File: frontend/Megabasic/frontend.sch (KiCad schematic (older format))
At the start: 26 parts, among them CN1 EDGE, J1 CONN_02X01, J2 CONN_02X01, P1 CONN_01X02, P2 CONN_01X02, P3 CONN_01X12, P4 Control for Megaband, Q1 FDV301, T1 4:1, T2 8:1, U1 4050, U2 74LS145

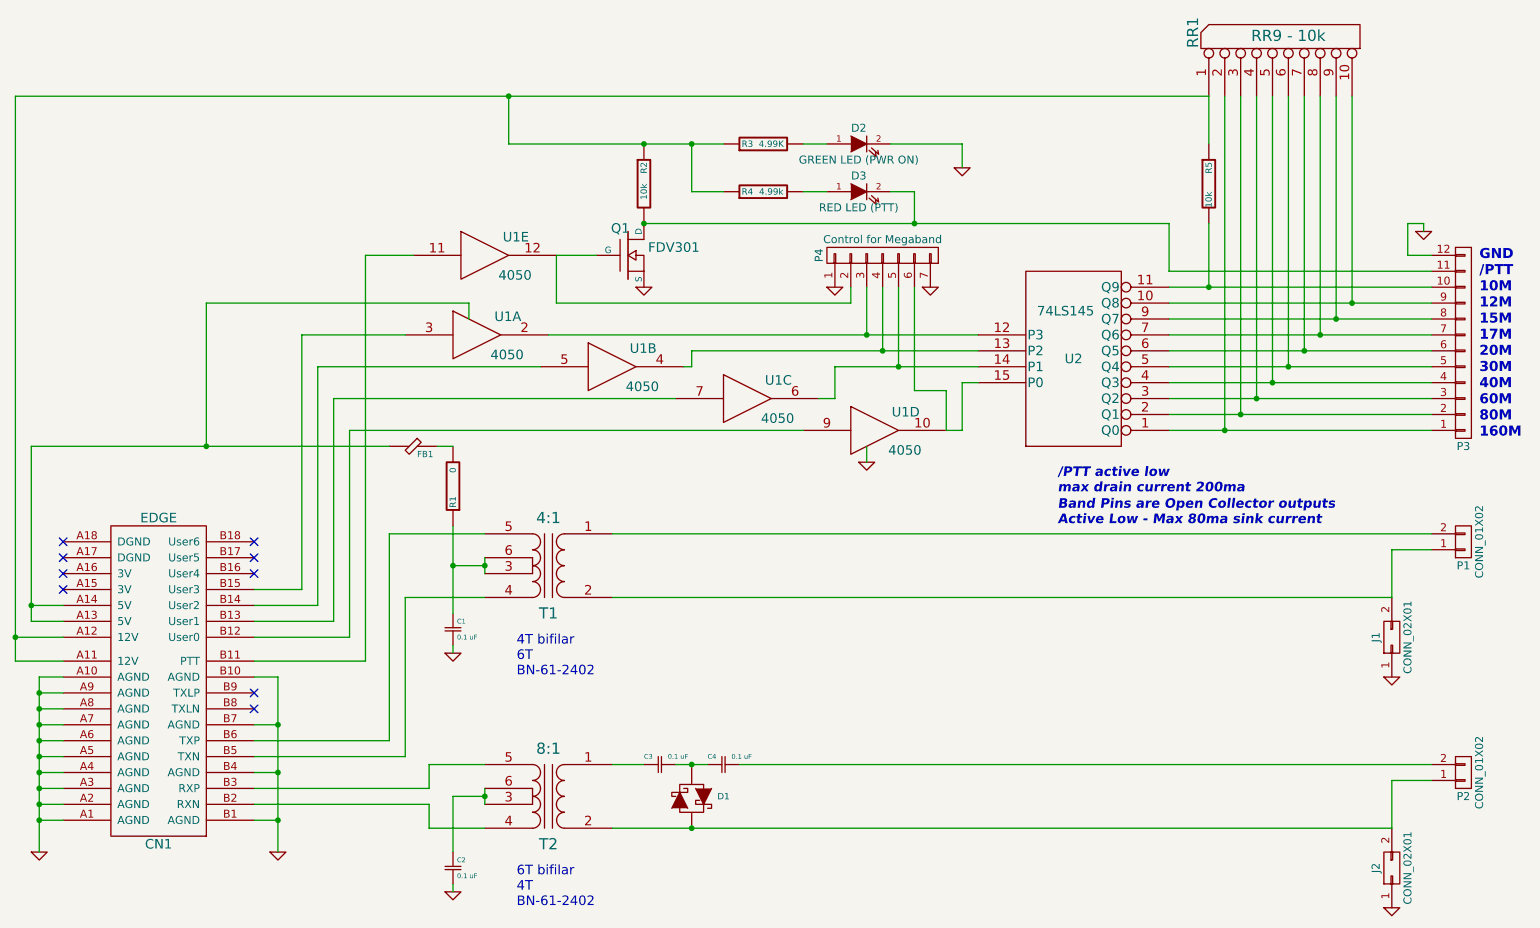
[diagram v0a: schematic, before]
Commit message: Further updates to the pre-V2 amp
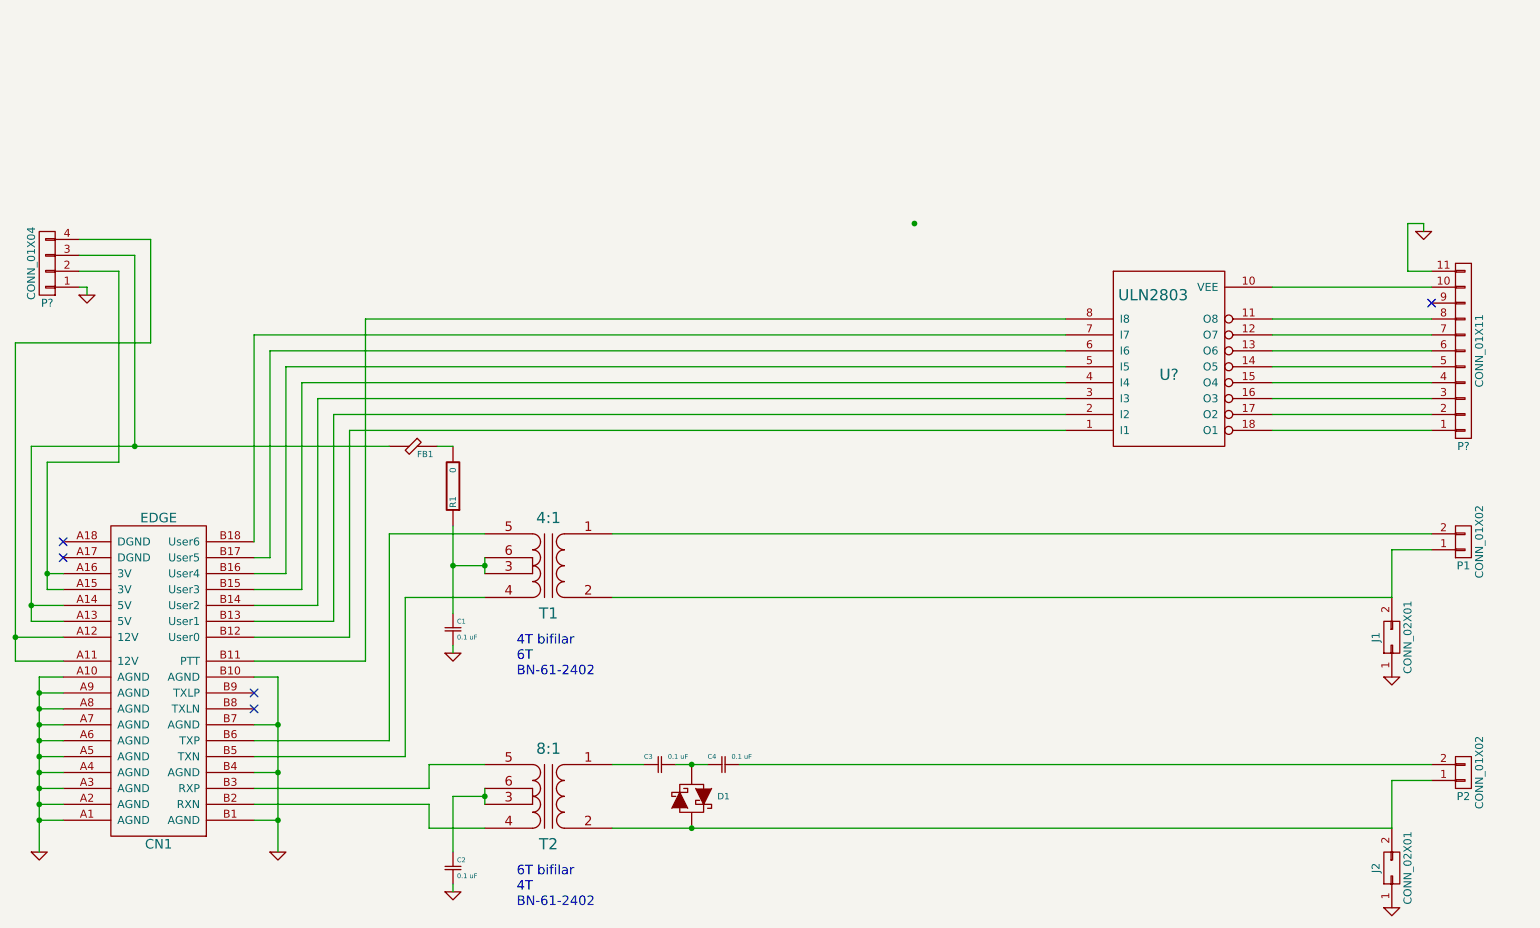
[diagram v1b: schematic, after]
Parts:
- removed D2: GREEN LED (PWR ON), LEDs:LED-0805, symbol LED
- removed D3: RED LED (PTT), LEDs:LED-0805, symbol LED
- removed P3: CONN_01X12, Pin_Headers:Pin_Header_Straight_1x12, symbol CONN_01X12
- removed P4: Control for Megaband, Pin_Headers:Pin_Header_Straight_1x07, symbol CONN_01X07
- removed Q1: FDV301, HERMESLITE:SOT-23-GDS, symbol MOSFET_N
- removed R2, R5: 10k, Resistors_SMD:R_0805_HandSoldering, symbol R
- removed R3: 4.99K, Resistors_SMD:R_0805_HandSoldering, symbol R
- removed R4: 4.99k, Resistors_SMD:R_0805_HandSoldering, symbol R
- removed RR1: RR9 - 10k, Discret:r_pack9, symbol RR9
- removed U1: 4050, Housings_SOIC:SOIC-16_3.9x9.9mm_Pitch1.27mm, symbol 4050
- removed U2: 74LS145, Housings_SOIC:SOIC-16_3.9x9.9mm_Pitch1.27mm, symbol 74LS145
- added P?: CONN_01X04, symbol CONN_01X04
- added P?: CONN_01X11, symbol CONN_01X11
- added U?: ULN2803, symbol MC1417
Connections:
- net GND: now also P?.1 (P1), P?.11 (P11), U?.9 (GND)
- net at CN1.A11 (12V), CN1.A12 (12V): now also P?.4 (P4)
- net at CN1.A15 (3V): now also CN1.A16 (3V), P?.2 (P2)
- net at CN1.B11 (PTT): now also U?.8 (I8)
- net at CN1.B12 (User0): now also U?.1 (I1)
- net at CN1.B13 (User1): now also U?.2 (I2)
- net at CN1.B14 (User2): now also U?.3 (I3)
- net at CN1.B15 (User3): now also U?.4 (I4)
- net at CN1.B16 (User4): now also U?.5 (I5)
- net at CN1.B17 (User5): now also U?.6 (I6)
- net at CN1.B18 (User6): now also U?.7 (I7)
- net VCC: no longer names the net of CN1.A13 (5V), CN1.A14 (5V), FB1.1
- net VCC: now also P?.3 (P3)
- new net: P?.10 (P10), U?.10 (VEE)
- new net: P?.8 (P8), U?.11 (O8)
- new net: P?.7 (P7), U?.12 (O7)
- new net: P?.6 (P6), U?.13 (O6)
- new net: P?.5 (P5), U?.14 (O5)
- new net: P?.4 (P4), U?.15 (O4)
- new net: P?.3 (P3), U?.16 (O3)
- new net: P?.2 (P2), U?.17 (O2)
- new net: P?.1 (P1), U?.18 (O1)
- no-connect marks 9 -> 5
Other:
- note removed: "/PTT active low\nmax drain current 200ma"
- note removed: "Band Pins are Open Collector outputs\nActive Low - Max 80ma sink current"
- note removed: "GND\n/PTT\n10M\n12M\n15M\n17M\n20M\n30M\n40M\n60M\n80M\n160M"

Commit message: v2rx changes and update to new kicad
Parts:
- R1: symbol R -> R-RESCUE-frontend
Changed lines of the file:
@@
 EESchema Schematic File Version 2
+LIBS:frontend-rescue
 LIBS:power
 LIBS:device
@@
 LIBS:memory
 LIBS:xilinx
-LIBS:special
 LIBS:microcontrollers
 LIBS:dsp
@@
 $EndComp
 $Comp
-L R R1
+L R-RESCUE-frontend R1
 U 1 1 5443441E
 P 3800 3800
@@
 Connection ~ 5300 5950
 $Comp
-L GND #PWR01
+L GND-RESCUE-frontend #PWR01
 U 1 1 544349E4
 P 3800 4850
@@
 $EndComp
 $Comp
-L GND #PWR02
+L GND-RESCUE-frontend #PWR02
 U 1 1 544349F8
 P 3800 6350
@@
 $EndComp
 $Comp
-L GND #PWR03
+L GND-RESCUE-frontend #PWR03
 U 1 1 54434A20
 P 1200 6100
@@
 	2550 5400 3400 5400
 $Comp
-L GND #PWR04
+L GND-RESCUE-frontend #PWR04
 U 1 1 54434F94
 P 2700 6100
@@
 	9900 2150 9900 2200
 $Comp
-L GND #PWR07
+L GND-RESCUE-frontend #PWR07
 U 1 1 54DF8781
 P 9900 2200
@@
 $EndComp
 $Comp
-L GND #PWR09
+L GND-RESCUE-frontend #PWR09
 U 1 1 5516B151
 P 9700 6450
@@
 $EndComp
 $Comp
-L GND #PWR010
+L GND-RESCUE-frontend #PWR010
 U 1 1 5516B48F
 P 9700 5000
@@
 $EndComp
 $Comp
-L GND #PWR?
+L GND-RESCUE-frontend #PWR?
 U 1 1 55D2FB0E
 P 1500 2600
